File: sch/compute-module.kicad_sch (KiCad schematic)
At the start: 8 parts, among them J1 Conn_02x20_Odd_Even, J3 Conn_02x07_Odd_Even, SW1 SW_Push

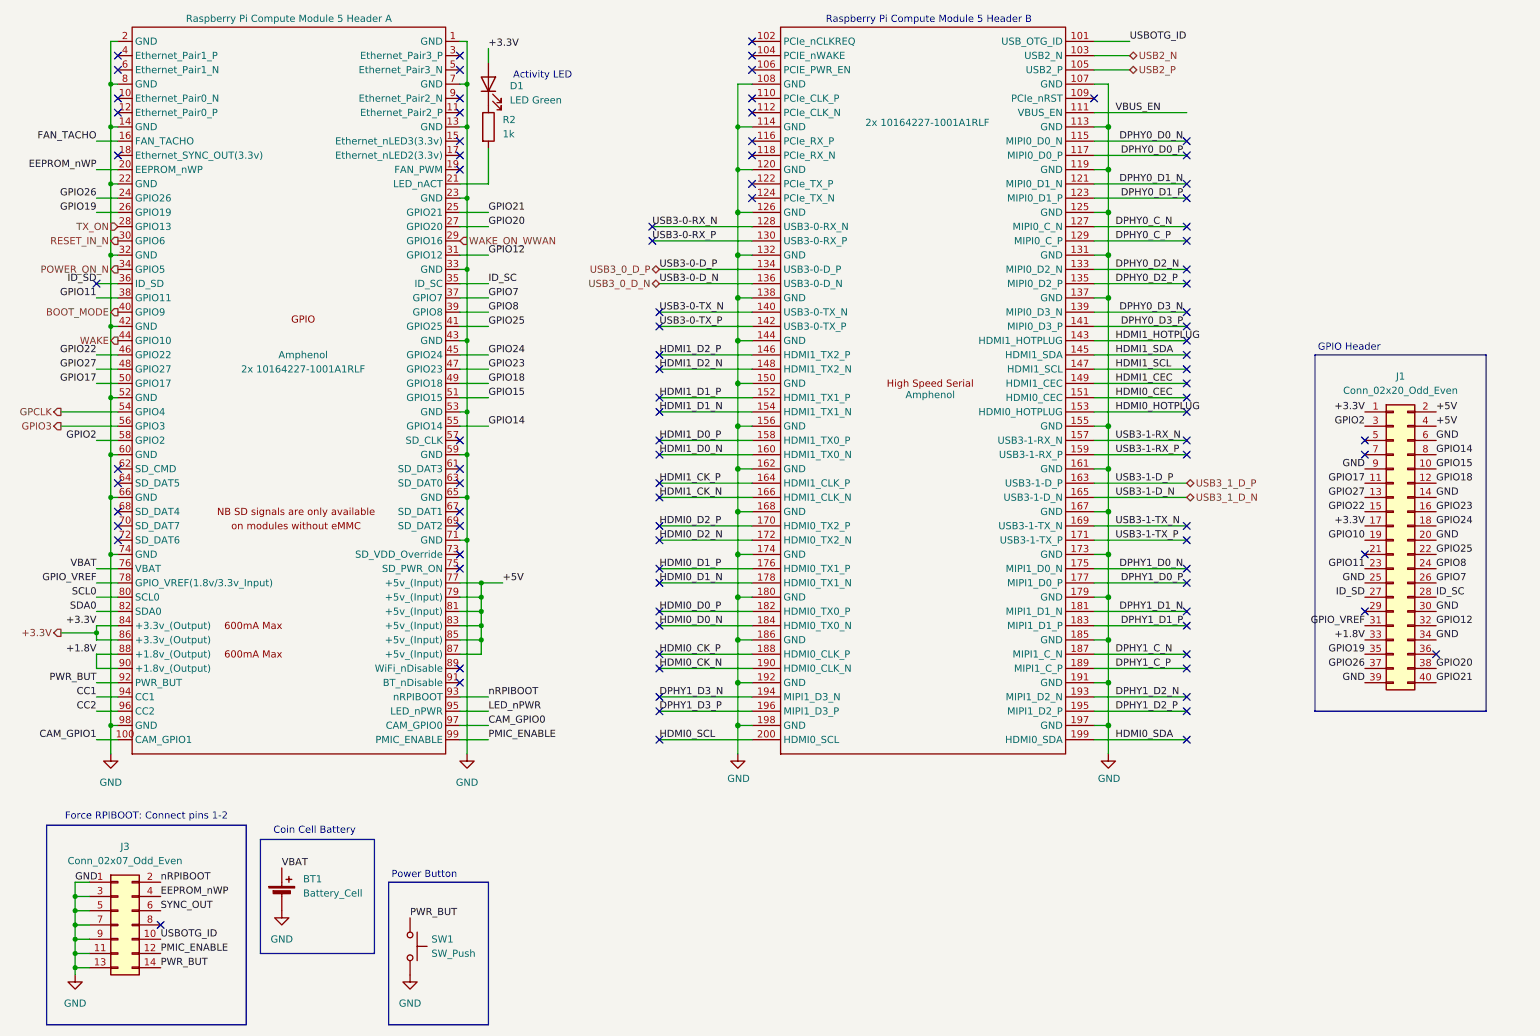
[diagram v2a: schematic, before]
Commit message: All pins connected
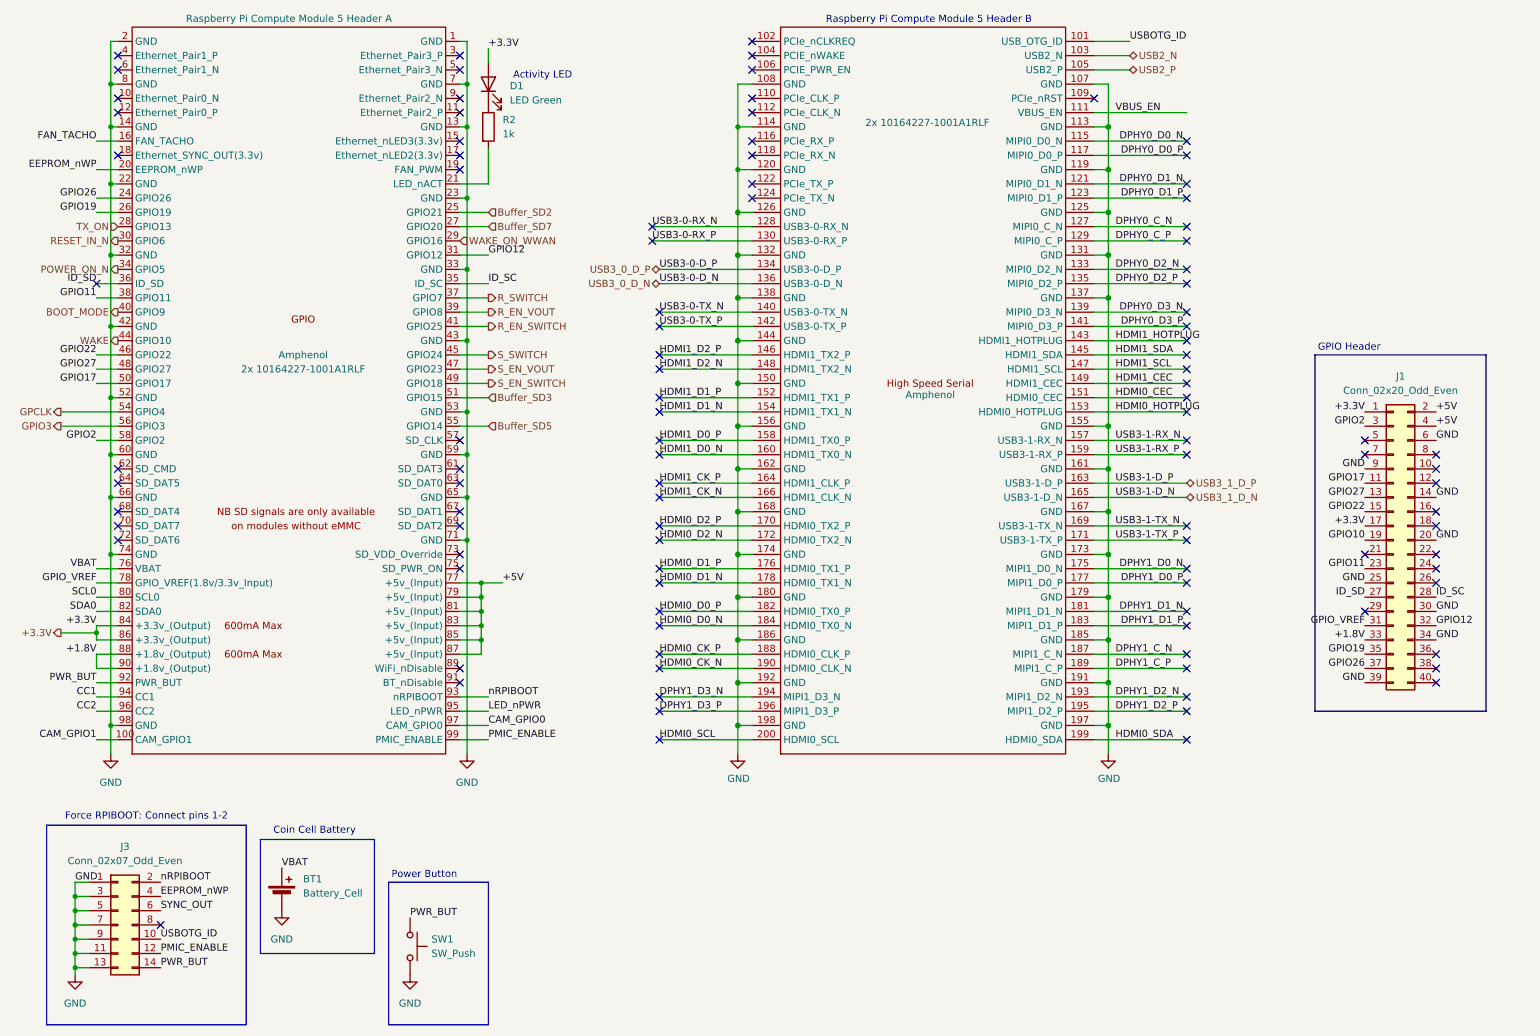
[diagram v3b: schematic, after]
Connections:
- net GPIO14: no longer names the net of J1.8 (Pin_8)
- net GPIO14: no longer Module1.55 (GPIO14)
- net GPIO15: no longer names the net of J1.10 (Pin_10)
- net GPIO15: no longer Module1.51 (GPIO15)
- net GPIO18: no longer names the net of J1.12 (Pin_12)
- net GPIO18: no longer Module1.49 (GPIO18)
- net GPIO20: no longer names the net of J1.38 (Pin_38)
- net GPIO20: no longer Module1.27 (GPIO20)
- net GPIO21: no longer names the net of J1.40 (Pin_40)
- net GPIO21: no longer Module1.25 (GPIO21)
- net GPIO23: no longer names the net of J1.16 (Pin_16)
- net GPIO23: no longer Module1.47 (GPIO23)
- net GPIO24: no longer names the net of J1.18 (Pin_18)
- net GPIO24: no longer Module1.45 (GPIO24)
- net GPIO25: no longer names the net of J1.22 (Pin_22)
- net GPIO25: no longer Module1.41 (GPIO25)
- net GPIO7: no longer names the net of J1.26 (Pin_26)
- net GPIO7: no longer Module1.37 (GPIO7)
- net GPIO8: no longer names the net of J1.24 (Pin_24)
- net GPIO8: no longer Module1.39 (GPIO8)
- new net Buffer_SD2: Module1.25 (GPIO21)
- new net Buffer_SD3: Module1.51 (GPIO15)
- new net Buffer_SD5: Module1.55 (GPIO14)
- new net Buffer_SD7: Module1.27 (GPIO20)
- new net R_EN_SWITCH: Module1.41 (GPIO25)
- new net R_EN_VOUT: Module1.39 (GPIO8)
- new net R_SWITCH: Module1.37 (GPIO7)
- new net S_EN_SWITCH: Module1.49 (GPIO18)
- new net S_EN_VOUT: Module1.47 (GPIO23)
- new net S_SWITCH: Module1.45 (GPIO24)
- no-connect marks 95 -> 105
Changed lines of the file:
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@@
 	)
 	(no_connect
+		(at 265.43 116.84)
+	)
+	(no_connect
 		(at 30.48 96.52)
 	)
@@
 	)
 	(no_connect
+		(at 265.43 99.06)
+	)
+	(no_connect
 		(at 220.98 71.12)
 	)
 	(no_connect
+		(at 265.43 106.68)
+	)
+	(no_connect
 		(at 91.44 40.64)
 	)
@@
 	)
 	(no_connect
+		(at 265.43 93.98)
+	)
+	(no_connect
 		(at 127 144.78)
 	)
@@
 	)
 	(no_connect
+		(at 265.43 96.52)
+	)
+	(no_connect
+		(at 265.43 104.14)
+	)
+	(no_connect
 		(at 91.44 25.4)
 	)
@@
 	)
 	(no_connect
+		(at 265.43 132.08)
+	)
+	(no_connect
 		(at 220.98 137.16)
 	)
@@
 	)
 	(no_connect
+		(at 265.43 111.76)
+	)
+	(no_connect
 		(at 91.44 99.06)
 	)
@@
 	)
 	(no_connect
+		(at 265.43 114.3)
+	)
+	(no_connect
 		(at 143.51 25.4)
 	)
@@
 	)
 	(no_connect
+		(at 265.43 134.62)
+	)
+	(no_connect
 		(at 127 101.6)
 	)
@@
 		)
 	)
-	(label "GPIO21"
-		(at 265.43 134.62 0)
-		(effects
-			(font
-				(size 1.27 1.27)
-			)
-			(justify left bottom)
-		)
-	)
-	(label "GPIO25"
-		(at 265.43 111.76 0)
-		(effects
-			(font
-				(size 1.27 1.27)
-			)
-			(justify left bottom)
-		)
-	)
 	(label "USB3-0-TX_N"
 		(at 127 68.58 0)
@@
 		)
 	)
-	(label "GPIO18"
-		(at 265.43 99.06 0)
-		(effects
-			(font
-				(size 1.27 1.27)
-			)
-			(justify left bottom)
-		)
-	)
 	(label "CC1"
 		(at 26.67 137.16 180)
@@
 		)
 	)
-	(label "GPIO21"
-		(at 96.52 50.8 0)
-		(effects
-			(font
-				(size 1.27 1.27)
-			)
-			(justify left bottom)
-		)
-	)
 	(label "+1.8V"
 		(at 252.73 127 180)
@@
 		)
 	)
-	(label "GPIO7"
-		(at 96.52 66.04 0)
-		(effects
-			(font
-				(size 1.27 1.27)
-			)
-			(justify left bottom)
-		)
-	)
 	(label "+5V"
 		(at 99.06 116.84 0)
@@
 		)
 	)
-	(label "GPIO14"
-		(at 265.43 93.98 0)
-		(effects
-			(font
-				(size 1.27 1.27)
-			)
-			(justify left bottom)
-		)
-	)
 	(label "HDMI1_D2_P"
 		(at 127 76.2 0)
@@
 		)
 	)
-	(label "GPIO8"
-		(at 265.43 114.3 0)
-		(effects
-			(font
-				(size 1.27 1.27)
-			)
-			(justify left bottom)
-		)
-	)
 	(label "USBOTG_ID"
 		(at 38.1 180.34 0)
@@
 		)
 	)
-	(label "GPIO23"
-		(at 265.43 104.14 0)
-		(effects
-			(font
-				(size 1.27 1.27)
-			)
-			(justify left bottom)
-		)
-	)
 	(label "DPHY1_C_N"
 		(at 208.28 129.54 0)
@@
 		)
 	)
-	(label "GPIO15"
-		(at 96.52 83.82 0)
-		(effects
-			(font
-				(size 1.27 1.27)
-			)
-			(justify left bottom)
-		)
-	)
 	(label "HDMI0_D1_N"
 		(at 127 116.84 0)
@@
 		)
 	)
-	(label "GPIO23"
-		(at 96.52 78.74 0)
-		(effects
-			(font
-				(size 1.27 1.27)
-			)
-			(justify left bottom)
-		)
-	)
 	(label "HDMI1_D2_N"
 		(at 127 78.74 0)
@@
 		)
 	)
-	(label "GPIO20"
-		(at 265.43 132.08 0)
-		(effects
-			(font
-				(size 1.27 1.27)
-			)
-			(justify left bottom)
-		)
-	)
 	(label "USB3-0-RX_P"
 		(at 125.73 55.88 0)
@@
 		)
 	)
-	(label "GPIO24"
-		(at 96.52 76.2 0)
-		(effects
-			(font
-				(size 1.27 1.27)
-			)
-			(justify left bottom)
-		)
-	)
-	(label "GPIO25"
-		(at 96.52 71.12 0)
-		(effects
-			(font
-				(size 1.27 1.27)
-			)
-			(justify left bottom)
-		)
-	)
 	(label "USB3-1-RX_N"
 		(at 208.28 91.44 0)
@@
 		)
 	)
-	(label "GPIO20"
-		(at 96.52 53.34 0)
-		(effects
-			(font
-				(size 1.27 1.27)
-			)
-			(justify left bottom)
-		)
-	)
 	(label "DPHY1_C_P"
 		(at 208.28 132.08 0)
@@
 		)
 	)
-	(label "GPIO18"
-		(at 96.52 81.28 0)
-		(effects
-			(font
-				(size 1.27 1.27)
-			)
-			(justify left bottom)
-		)
-	)
-	(label "GPIO7"
-		(at 265.43 116.84 0)
-		(effects
-			(font
-				(size 1.27 1.27)
-			)
-			(justify left bottom)
-		)
-	)
 	(label "USB3-1-D_P"
 		(at 208.28 99.06 0)
@@
 		)
 	)
-	(label "GPIO24"
-		(at 265.43 106.68 0)
-		(effects
-			(font
-				(size 1.27 1.27)
-			)
-			(justify left bottom)
-		)
-	)
 	(label "VBUS_EN"
 		(at 208.28 33.02 0)
@@
 		)
 	)
-	(label "GPIO15"
-		(at 265.43 96.52 0)
-		(effects
-			(font
-				(size 1.27 1.27)
-			)
-			(justify left bottom)
-		)
-	)
 	(label "DPHY0_D2_P"
 		(at 208.28 63.5 0)
@@
 		)
 	)
-	(label "GPIO8"
-		(at 96.52 68.58 0)
+	(label "GPIO26"
+		(at 252.73 132.08 180)
 		(effects
 			(font
 				(size 1.27 1.27)
 			)
-			(justify left bottom)
+			(justify right bottom)
 		)
 	)
-	(label "GPIO26"
-		(at 252.73 132.08 180)
+	(hierarchical_label "USB3_0_D_N"
+		(shape bidirectional)
+		(at 127 63.5 180)
 		(effects
 			(font
 				(size 1.27 1.27)
 			)
-			(justify right bottom)
+			(justify right)
 		)
 	)
-	(label "GPIO14"
-		(at 96.52 88.9 0)
+	(hierarchical_label "R_EN_SWITCH"
+		(shape output)
+		(at 96.52 71.12 0)
 		(effects
 			(font
 				(size 1.27 1.27)
 			)
-			(justify left bottom)
+			(justify left)
 		)
 	)
-	(hierarchical_label "USB3_0_D_N"
-		(shape bidirectional)
-		(at 127 63.5 180)
+	(hierarchical_label "WAKE_ON_WWAN"
+		(shape input)
+		(at 91.44 55.88 0)
 		(effects
 			(font
 				(size 1.27 1.27)
 			)
-			(justify right)
+			(justify left)
 		)
 	)
-	(hierarchical_label "WAKE_ON_WWAN"
+	(hierarchical_label "Buffer_SD3"
 		(shape input)
-		(at 91.44 55.88 0)
+		(at 96.52 83.82 0)
+		(effects
+			(font
+				(size 1.27 1.27)
+			)
+			(justify left)
+		)
+	)
+	(hierarchical_label "S_EN_SWITCH"
+		(shape output)
+		(at 96.52 81.28 0)
+		(effects
+			(font
+				(size 1.27 1.27)
+			)
+			(justify left)
+		)
+	)
+	(hierarchical_label "Buffer_SD7"
+		(shape input)
+		(at 96.52 53.34 0)
 		(effects
 			(font
@@
 		)
 	)
+	(hierarchical_label "R_EN_VOUT"
+		(shape output)
+		(at 96.52 68.58 0)
+		(effects
+			(font
+				(size 1.27 1.27)
+			)
+			(justify left)
+		)
+	)
 	(hierarchical_label "USB3_0_D_P"
 		(shape bidirectional)
@@
 		)
 	)
+	(hierarchical_label "R_SWITCH"
+		(shape output)
+		(at 96.52 66.04 0)
+		(effects
+			(font
+				(size 1.27 1.27)
+			)
+			(justify left)
+		)
+	)
+	(hierarchical_label "S_EN_VOUT"
+		(shape output)
+		(at 96.52 78.74 0)
+		(effects
+			(font
+				(size 1.27 1.27)
+			)
+			(justify left)
+		)
+	)
+	(hierarchical_label "Buffer_SD2"
+		(shape input)
+		(at 96.52 50.8 0)
+		(effects
+			(font
+				(size 1.27 1.27)
+			)
+			(justify left)
+		)
+	)
 	(hierarchical_label "USB3_1_D_N"
 		(shape bidirectional)
@@
 		(effects
 			(font
+				(size 1.27 1.27)
+			)
+			(justify left)
+		)
+	)
+	(hierarchical_label "S_SWITCH"
+		(shape output)
+		(at 96.52 76.2 0)
+		(effects
+			(font
+				(size 1.27 1.27)
+			)
+			(justify left)
+		)
+	)
+	(hierarchical_label "Buffer_SD5"
+		(shape input)
+		(at 96.52 88.9 0)
+		(effects
+			(font

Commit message: added cap footprints and part numbers
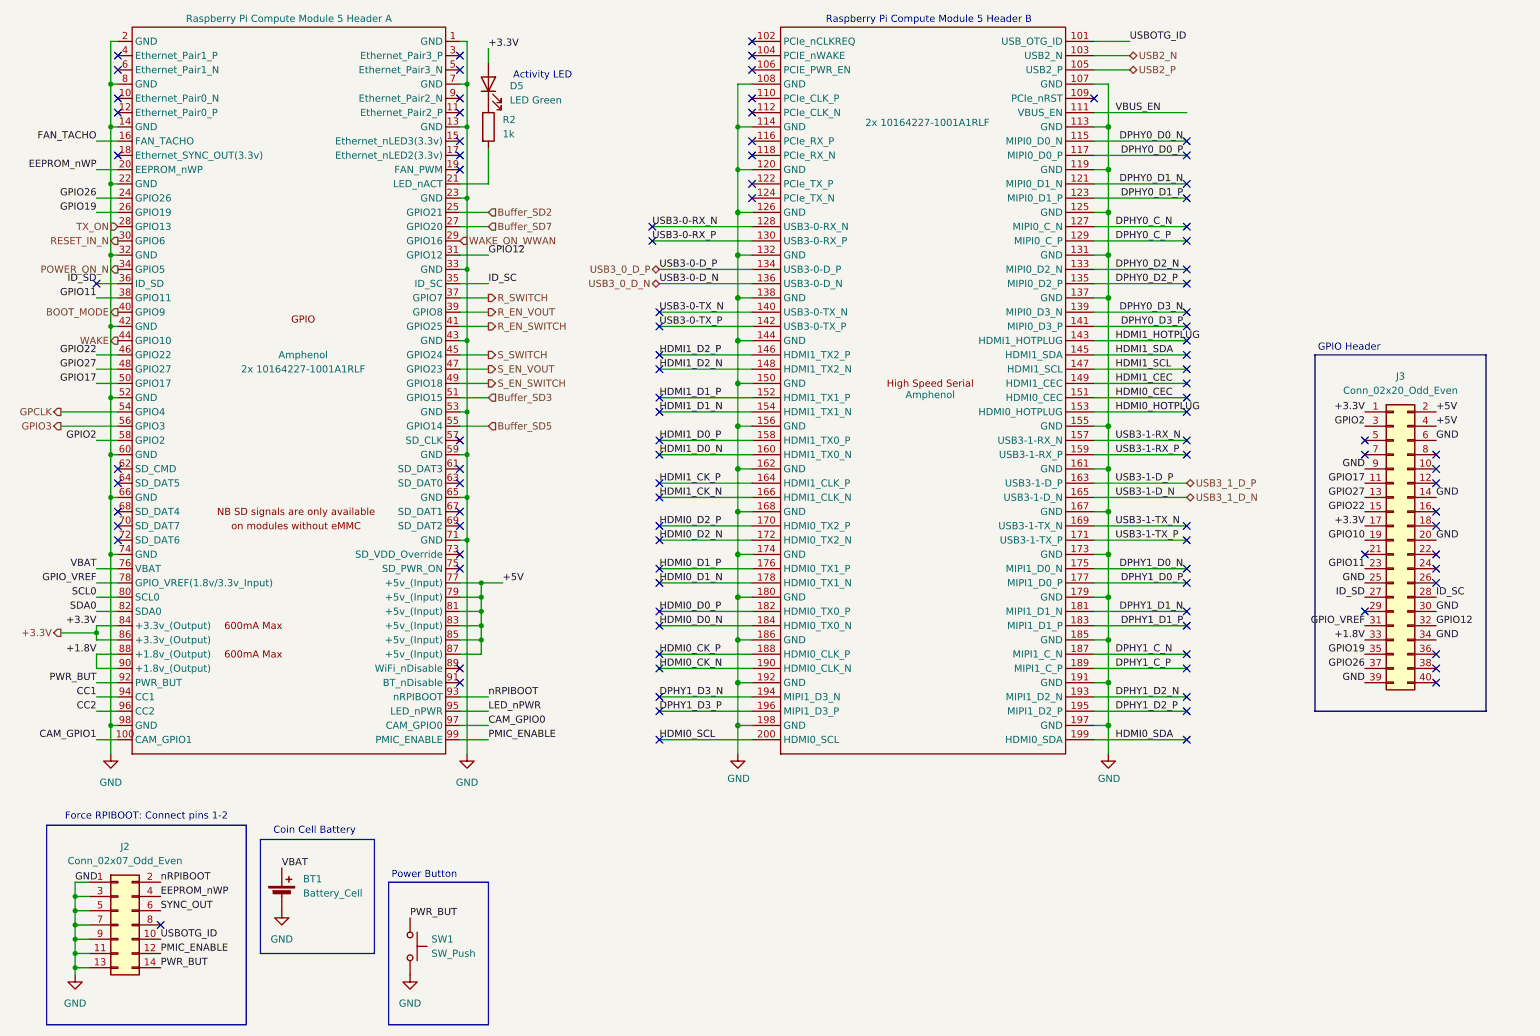
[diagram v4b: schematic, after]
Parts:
- renumbered D1 to D5, J3 to J2, J1 to J3, Module2 to Module1, Module1 to Module2
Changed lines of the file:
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@@
 		(on_board yes)
 		(dnp no)
-		(property "Reference" "#PWR0130"
+		(property "Reference" "#PWR014"
 			(at 207.01 153.67 0)
 			(effects
@@
 			(project "audiograb"
 				(path "/c46c2311-6d4b-411d-b012-c7730eac136d/75b669f4-4784-4707-8d6c-b4da66be0510"
-					(reference "#PWR0130")
+					(reference "#PWR014")
 					(unit 1)
 				)
@@
 		(on_board yes)
 		(dnp no)
-		(property "Reference" "#PWR0131"
+		(property "Reference" "#PWR013"
 			(at 140.97 153.67 0)
 			(effects
@@
 			(project "audiograb"
 				(path "/c46c2311-6d4b-411d-b012-c7730eac136d/75b669f4-4784-4707-8d6c-b4da66be0510"
-					(reference "#PWR0131")
+					(reference "#PWR013")
 					(unit 1)
 				)
@@
 		(on_board yes)
 		(dnp no)
-		(property "Reference" "Module1"
+		(property "Reference" "Module2"
 			(at 60.96 14.224 0)
 			(effects
@@
 			(project "audiograb"
 				(path "/c46c2311-6d4b-411d-b012-c7730eac136d/75b669f4-4784-4707-8d6c-b4da66be0510"
-					(reference "Module1")
+					(reference "Module2")
 					(unit 1)
 				)
@@
 		(dnp no)
 		(fields_autoplaced yes)
-		(property "Reference" "J1"
+		(property "Reference" "J3"
 			(at 259.08 80.01 0)
 			(effects
@@
 			(project ""
 				(path "/c46c2311-6d4b-411d-b012-c7730eac136d/75b669f4-4784-4707-8d6c-b4da66be0510"
-					(reference "J1")
+					(reference "J3")
 					(unit 1)
 				)
@@
 		(dnp no)
 		(fields_autoplaced yes)
-		(property "Reference" "#PWR0101"
+		(property "Reference" "#PWR09"
 			(at 29.21 153.67 0)
 			(effects
@@
 			(project "audiograb"
 				(path "/c46c2311-6d4b-411d-b012-c7730eac136d/75b669f4-4784-4707-8d6c-b4da66be0510"
-					(reference "#PWR0101")
+					(reference "#PWR09")
 					(unit 1)
 				)
@@
 		(dnp no)
 		(fields_autoplaced yes)
-		(property "Reference" "J3"
+		(property "Reference" "J2"
 			(at 31.75 163.83 0)
 			(effects
@@
 			(project ""
 				(path "/c46c2311-6d4b-411d-b012-c7730eac136d/75b669f4-4784-4707-8d6c-b4da66be0510"
-					(reference "J3")
+					(reference "J2")
 					(unit 1)
 				)
@@
 		(dnp no)
 		(fields_autoplaced yes)
-		(property "Reference" "D1"
+		(property "Reference" "D5"
 			(at 100.33 28.2574 90)
 			(effects
@@
 			(project "audiograb"
 				(path "/c46c2311-6d4b-411d-b012-c7730eac136d/75b669f4-4784-4707-8d6c-b4da66be0510"
-					(reference "D1")
+					(reference "D5")
 					(unit 1)
 				)
@@
 		(dnp no)
 		(fields_autoplaced yes)
-		(property "Reference" "#PWR0102"
+		(property "Reference" "#PWR012"
 			(at 92.71 153.67 0)
 			(effects
@@
 			(project "audiograb"
 				(path "/c46c2311-6d4b-411d-b012-c7730eac136d/75b669f4-4784-4707-8d6c-b4da66be0510"
-					(reference "#PWR0102")
+					(reference "#PWR012")
 					(unit 1)
 				)
@@
 		(dnp no)
 		(fields_autoplaced yes)
-		(property "Reference" "#PWR09"
+		(property "Reference" "#PWR011"
 			(at 82.55 193.04 0)
 			(effects
@@
 			(project ""
 				(path "/c46c2311-6d4b-411d-b012-c7730eac136d/75b669f4-4784-4707-8d6c-b4da66be0510"
-					(reference "#PWR09")
+					(reference "#PWR011")
 					(unit 1)
 				)
@@
 		(on_board yes)
 		(dnp no)
-		(property "Reference" "Module2"
+		(property "Reference" "Module1"
 			(at 173.99 9.017 0)
 			(effects
@@
 			(project "audiograb"
 				(path "/c46c2311-6d4b-411d-b012-c7730eac136d/75b669f4-4784-4707-8d6c-b4da66be0510"
-					(reference "Module2")
+					(reference "Module1")
 					(unit 2)
 				)

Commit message: added footprints fore resistors
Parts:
- R2: footprint (none) -> Resistor_SMD:R_0603_1608Metric; MPN (none) -> RC0603FR-071KL
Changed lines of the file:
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@@
 			)
 		)
-		(property "Footprint" ""
+		(property "Footprint" "Resistor_SMD:R_0603_1608Metric"
 			(at 94.742 35.56 90)
 			(effects
@@
 			(at 96.52 35.56 0)
 			(effects
+				(font
+					(size 1.27 1.27)
+				)
+				(hide yes)
+			)
+		)
+		(property "MPN" "RC0603FR-071KL"
+			(at 96.52 35.56 0)
+			(effects
